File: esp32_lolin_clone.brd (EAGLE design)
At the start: 25 x 58 mm, 33 parts, among them J1 10104111-0001LF, P1 S2B-PH-SM4-TB, Q1 CJ2301S1, Q2 CJ2301S1, SW1 PTS815SJK250SMTR, U1 ESP32-WROOM-32D, U2 BCM857, U3 ME6211, U4 UMH3N, U5 TP4054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

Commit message: - Finish BOM, modify BOM related issues in schematic.
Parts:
- JP2: value (none) -> 1X20_SMALLPAD
- LED1, LED2: value (none) -> WHITE
- R6, R9: value 2K -> 2K2
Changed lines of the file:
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@@
 </element>
 <element name="U1" library="ML_badge" package="MODULE_ESP32-WROOM-32D" value="ESP32-WROOM-32D" x="12.5" y="45.41" smashed="yes">
-<attribute name="AVAILABILITY" value="Unavailable" x="35.36" y="28.9" size="1.778" layer="27" display="off"/>
 <attribute name="DISTRIBUTOR" value="Mouser" x="35.36" y="28.9" size="1.778" layer="27" display="off"/>
-<attribute name="DISTRUBUTOR_REF" value="356-ESP32WROOM-32D" x="35.36" y="28.9" size="1.778" layer="27" display="off"/>
+<attribute name="DISTRIBUTOR_REF" value="356-ESP32WROOM-32D" x="12.5" y="45.41" size="1.778" layer="27" display="off"/>
 <attribute name="MANUFACTURER" value="Espressif Systems" x="35.36" y="28.9" size="1.778" layer="27" display="off"/>
 <attribute name="MANUFACTURER_REF" value="ESP32-WROOM-32D" x="35.36" y="28.9" size="1.778" layer="27" display="off"/>
@@
 </element>
 <element name="U6" library="RE_wemos_lolin_clone" package="QFN50P400X400X80-25N" value="CP2104-F03-GM" x="17.6" y="11.6" smashed="yes">
+<attribute name="DISTRIBUTOR" value="Mouser" x="17.6" y="11.6" size="1.778" layer="27" display="off"/>
 <attribute name="DISTRIBUTOR_REF" value="None" x="17.6" y="11.6" size="1.778" layer="27" display="off"/>
-<attribute name="DISTRUBUTOR" value="Mouser" x="17.6" y="11.6" size="1.778" layer="27" display="off"/>
 <attribute name="MANUFACTURER" value="Silabs" x="17.6" y="11.6" size="1.778" layer="27" display="off"/>
 <attribute name="MANUFACTURER_REF" value="CP2104" x="17.6" y="11.6" size="1.778" layer="27" display="off"/>
@@
 <attribute name="VALUE" x="19.805" y="17.965" size="1.27" layer="27" rot="R90"/>
 </element>
-<element name="LED2" library="led" library_urn="urn:adsk.eagle:library:259" package="CHIP-LED0603" package3d_urn="urn:adsk.eagle:package:15819/3" value="" x="12.4" y="23.6" smashed="yes" rot="R90">
+<element name="LED2" library="led" library_urn="urn:adsk.eagle:library:259" package="CHIP-LED0603" package3d_urn="urn:adsk.eagle:package:15819/3" value="WHITE" x="12.4" y="23.6" smashed="yes" rot="R90">
 <attribute name="NAME" x="13.435" y="22.865" size="0.7" layer="25" font="vector" ratio="15" rot="R180"/>
 <attribute name="POPULARITY" value="26" x="12.4" y="23.6" size="1.778" layer="27" rot="R90" display="off"/>
 <attribute name="VALUE" x="13.035" y="25.505" size="1.27" layer="27" rot="R180"/>
 </element>
-<element name="R9" library="rcl" library_urn="urn:adsk.eagle:library:334" package="R0603" package3d_urn="urn:adsk.eagle:package:23555/3" value="2K" x="15.3" y="23.6" smashed="yes" rot="R180">
+<element name="R9" library="rcl" library_urn="urn:adsk.eagle:library:334" package="R0603" package3d_urn="urn:adsk.eagle:package:23555/3" value="2K2" x="15.3" y="23.6" smashed="yes" rot="R180">
 <attribute name="NAME" x="15.835" y="22.765" size="0.7" layer="25" font="vector" ratio="15" rot="R180"/>
 <attribute name="POPULARITY" value="70" x="15.3" y="23.6" size="1.778" layer="27" rot="R180" display="off"/>
@@
 <attribute name="VALUE" x="-1.875" y="52.12" size="1.27" layer="27" rot="R270"/>
 </element>
-<element name="JP2" library="RE_wemos_lolin_clone" package="1X20" package3d_urn="urn:adsk.eagle:package:22441/2" value="" x="23.7" y="26.8" smashed="yes" rot="R270">
+<element name="JP2" library="RE_wemos_lolin_clone" package="1X20" value="1X20_SMALLPAD" x="23.7" y="26.8" smashed="yes" rot="R270">
 <attribute name="NAME" x="22.8238" y="52.5288" size="0.7" layer="25" font="vector" ratio="15"/>
-<attribute name="POPULARITY" value="6" x="23.7" y="26.8" size="1.778" layer="27" rot="R270" display="off"/>
 <attribute name="VALUE" x="20.525" y="52.2" size="1.27" layer="27" rot="R270"/>
 </element>
@@
 </element>
 <element name="P1" library="RE_wemos_lolin_clone" package="JST_S2B-PH-SM4-TB" value="S2B-PH-SM4-TB" x="8" y="5.7" smashed="yes" rot="R90">
-<attribute name="AVAILABILITY" value="Unavailable" x="8" y="5.7" size="1.778" layer="27" rot="R90" display="off"/>
-<attribute name="DESCRIPTION" value=" Connector Header Surface Mount, Right Angle 2 position 0.079 _2.00mm_ " x="8" y="5.7" size="1.778" layer="27" rot="R90" display="off"/>
-<attribute name="MF" value="JST Sales" x="8" y="5.7" size="1.778" layer="27" rot="R90" display="off"/>
-<attribute name="MP" value="S2B-PH-SM4-TB" x="8" y="5.7" size="1.778" layer="27" rot="R90" display="off"/>
+<attribute name="DISTRIBUTOR" value="Farnell" x="8" y="5.7" size="1.778" layer="27" rot="R90" display="off"/>
+<attribute name="DISTRIBUTOR_REF" value="9492615" x="8" y="5.7" size="1.778" layer="27" rot="R90" display="off"/>
+<attribute name="MANUFACTURER" value="JST Sales" x="8" y="5.7" size="1.778" layer="27" rot="R90" display="off"/>
+<attribute name="MANUFACTURER_REF" value="S2B-PH-SM4-TB" x="8" y="5.7" size="1.778" layer="27" rot="R90" display="off"/>
 <attribute name="NAME" x="6.19378125" y="2.261409375" size="1" layer="25" font="vector" ratio="15"/>
-<attribute name="PACKAGE" value="None" x="8" y="5.7" size="1.778" layer="27" rot="R90" display="off"/>
-<attribute name="PRICE" value="None" x="8" y="5.7" size="1.778" layer="27" rot="R90" display="off"/>
 <attribute name="VALUE" x="11.750990625" y="1.198809375" size="1.270340625" layer="27" rot="R90"/>
 </element>
@@
 <attribute name="VALUE" x="17.9" y="4.65" size="1.016" layer="27"/>
 </element>
-<element name="LED1" library="led" library_urn="urn:adsk.eagle:library:259" package="CHIP-LED0603" package3d_urn="urn:adsk.eagle:package:15819/3" value="" x="5.761" y="16.617" smashed="yes" rot="R90">
+<element name="LED1" library="led" library_urn="urn:adsk.eagle:library:259" package="CHIP-LED0603" package3d_urn="urn:adsk.eagle:package:15819/3" value="WHITE" x="5.761" y="16.617" smashed="yes" rot="R90">
 <attribute name="NAME" x="6.796" y="15.982" size="0.7" layer="25" font="vector" ratio="15" rot="R180"/>
 <attribute name="POPULARITY" value="26" x="5.761" y="16.617" size="1.778" layer="27" rot="R90" display="off"/>
 <attribute name="VALUE" x="6.396" y="18.522" size="1.27" layer="27" rot="R180"/>
 </element>
-<element name="R6" library="rcl" library_urn="urn:adsk.eagle:library:334" package="R0603" package3d_urn="urn:adsk.eagle:package:23555/3" value="2K" x="5.6" y="18" smashed="yes">
+<element name="R6" library="rcl" library_urn="urn:adsk.eagle:library:334" package="R0603" package3d_urn="urn:adsk.eagle:package:23555/3" value="2K2" x="5.6" y="18" smashed="yes">
 <attribute name="NAME" x="5.165" y="18.735" size="0.7" layer="25" font="vector" ratio="15"/>
 <attribute name="POPULARITY" value="70" x="5.6" y="18" size="1.778" layer="27" display="off"/>

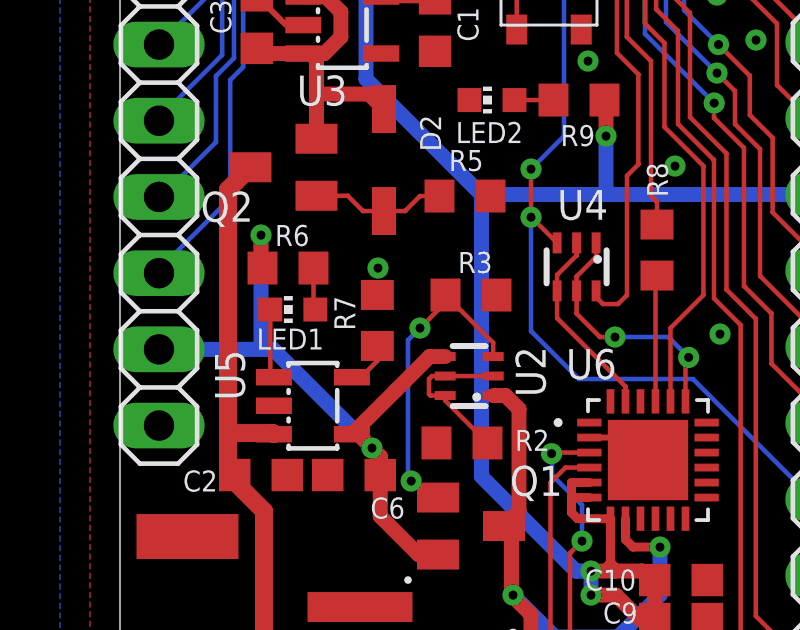
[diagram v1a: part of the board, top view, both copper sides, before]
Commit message: - Fix critical error 5V connection missing.
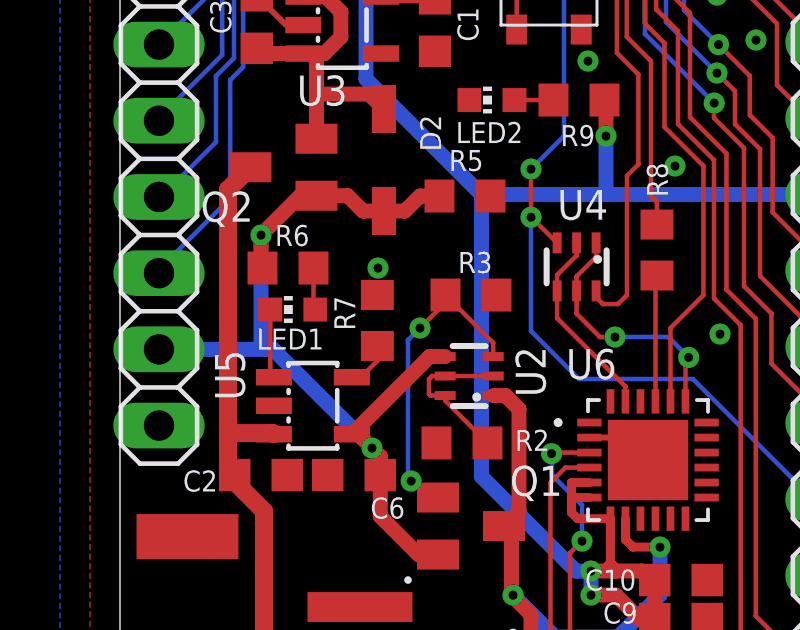
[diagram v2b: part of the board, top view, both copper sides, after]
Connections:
- removed net N$5: D2.2, Q2.1, R5.1
- net +5V: now also D2.2, Q2.1, R5.1
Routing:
- net +5V: track 23.3 -> 30.2 mm
- net N$5: track 5.09 -> 0.00 mm
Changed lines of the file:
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@@
 <drawing>
 <settings>
-<setting alwaysvectorfont="yes"/>
+<setting alwaysvectorfont="no"/>
 <setting verticaltext="up"/>
 </settings>
 <grid distance="0.1" unitdist="mm" unit="mm" style="lines" multiple="1" display="yes" altdistance="5" altunitdist="mil" altunit="mil"/>
 <layers>
-<layer number="1" name="Top" color="4" fill="1" visible="no" active="yes"/>
+<layer number="1" name="Top" color="4" fill="1" visible="yes" active="yes"/>
 <layer number="2" name="Route2" color="16" fill="1" visible="no" active="no"/>
 <layer number="3" name="Route3" color="17" fill="1" visible="no" active="no"/>
@@
 <layer number="14" name="Route14" color="22" fill="1" visible="no" active="no"/>
 <layer number="15" name="Route15" color="23" fill="1" visible="no" active="no"/>
-<layer number="16" name="Bottom" color="1" fill="1" visible="no" active="yes"/>
-<layer number="17" name="Pads" color="2" fill="1" visible="no" active="yes"/>
-<layer number="18" name="Vias" color="2" fill="1" visible="no" active="yes"/>
+<layer number="16" name="Bottom" color="1" fill="1" visible="yes" active="yes"/>
+<layer number="17" name="Pads" color="2" fill="1" visible="yes" active="yes"/>
+<layer number="18" name="Vias" color="2" fill="1" visible="yes" active="yes"/>
 <layer number="19" name="Unrouted" color="6" fill="1" visible="yes" active="yes"/>
 <layer number="20" name="Dimension" color="24" fill="1" visible="yes" active="yes"/>
 <layer number="21" name="tPlace" color="7" fill="1" visible="yes" active="yes"/>
-<layer number="22" name="bPlace" color="7" fill="1" visible="no" active="yes"/>
+<layer number="22" name="bPlace" color="7" fill="1" visible="yes" active="yes"/>
 <layer number="23" name="tOrigins" color="15" fill="1" visible="yes" active="yes"/>
-<layer number="24" name="bOrigins" color="15" fill="1" visible="no" active="yes"/>
+<layer number="24" name="bOrigins" color="15" fill="1" visible="yes" active="yes"/>
 <layer number="25" name="tNames" color="7" fill="1" visible="yes" active="yes"/>
-<layer number="26" name="bNames" color="7" fill="1" visible="no" active="yes"/>
+<layer number="26" name="bNames" color="7" fill="1" visible="yes" active="yes"/>
 <layer number="27" name="tValues" color="7" fill="1" visible="no" active="yes"/>
 <layer number="28" name="bValues" color="7" fill="1" visible="no" active="yes"/>
-<layer number="29" name="tStop" color="7" fill="3" visible="yes" active="yes"/>
+<layer number="29" name="tStop" color="7" fill="3" visible="no" active="yes"/>
 <layer number="30" name="bStop" color="7" fill="6" visible="no" active="yes"/>
 <layer number="31" name="tCream" color="7" fill="4" visible="no" active="yes"/>
@@
 <layer number="38" name="bTest" color="7" fill="1" visible="no" active="yes"/>
 <layer number="39" name="tKeepout" color="4" fill="11" visible="yes" active="yes"/>
-<layer number="40" name="bKeepout" color="1" fill="11" visible="no" active="yes"/>
+<layer number="40" name="bKeepout" color="1" fill="11" visible="yes" active="yes"/>
 <layer number="41" name="tRestrict" color="4" fill="10" visible="yes" active="yes"/>
 <layer number="42" name="bRestrict" color="1" fill="10" visible="yes" active="yes"/>
@@
 <layer number="50" name="dxf" color="7" fill="1" visible="no" active="no"/>
 <layer number="51" name="tDocu" color="7" fill="1" visible="yes" active="yes"/>
-<layer number="52" name="bDocu" color="7" fill="1" visible="no" active="yes"/>
+<layer number="52" name="bDocu" color="7" fill="1" visible="yes" active="yes"/>
 <layer number="53" name="tGND_GNDA" color="7" fill="1" visible="no" active="no"/>
 <layer number="54" name="bGND_GNDA" color="7" fill="1" visible="no" active="no"/>
@@
 <wire x1="4.8" y1="15.29" x2="4.7" y2="15.39" width="0.5" layer="16"/>
 <wire x1="4.7" y1="15.39" x2="4.7" y2="19.1" width="0.5" layer="16"/>
-<wire x1="7.7301" y1="12.46" x2="9.18505" y2="13.91495" width="0.5" layer="1"/>
-<wire x1="9.18505" y1="13.91495" x2="10.3201" y2="15.05" width="0.5" layer="1"/>
+<wire x1="7.7301" y1="12.46" x2="10.3201" y2="15.05" width="0.5" layer="1"/>
 <wire x1="10.3201" y1="15.05" x2="10.84" y2="15.05" width="0.5" layer="1"/>
+<contactref element="D2" pad="2"/>
+<contactref element="R5" pad="1"/>
+<contactref element="Q2" pad="1"/>
+<wire x1="8.8" y1="19.9" x2="8.1" y2="19.9" width="0.5" layer="1"/>
+<wire x1="7.59" y1="20.41" x2="6.549" y2="20.41" width="0.5" layer="1"/>
+<wire x1="8.1" y1="19.9" x2="7.59" y2="20.41" width="0.5" layer="1"/>
+<wire x1="8.8" y1="19.9" x2="9.5" y2="19.9" width="0.5" layer="1"/>
+<wire x1="10" y1="20.4" x2="10.65" y2="20.4" width="0.5" layer="1"/>
+<wire x1="9.5" y1="19.9" x2="10" y2="20.4" width="0.5" layer="1"/>
+<wire x1="4.7" y1="19.1" x2="6.01" y2="20.41" width="0.5" layer="1"/>
+<wire x1="6.01" y1="20.41" x2="6.549" y2="20.41" width="0.5" layer="1"/>
 </signal>
 <signal name="IO2">
@@
 <wire x1="8.3" y1="23.8" x2="6.549" y2="23.8" width="0.5" layer="1"/>
 </signal>
-<signal name="N$5">
-<contactref element="D2" pad="2"/>
-<contactref element="R5" pad="1"/>
-<contactref element="Q2" pad="1"/>
-<wire x1="10.65" y1="20.4" x2="10.25" y2="20" width="0.1524" layer="1"/>
-<wire x1="8.8" y1="19.9" x2="8.1" y2="19.9" width="0.1524" layer="1"/>
-<wire x1="7.59" y1="20.41" x2="6.549" y2="20.41" width="0.1524" layer="1"/>
-<wire x1="8.1" y1="19.9" x2="7.59" y2="20.41" width="0.1524" layer="1"/>
-<wire x1="8.8" y1="19.9" x2="9.5" y2="19.9" width="0.1524" layer="1"/>
-<wire x1="10" y1="20.4" x2="10.65" y2="20.4" width="0.1524" layer="1"/>
-<wire x1="9.5" y1="19.9" x2="10" y2="20.4" width="0.1524" layer="1"/>
-</signal>
 <signal name="VBAT" class="4">
